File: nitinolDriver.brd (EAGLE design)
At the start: 25 parts

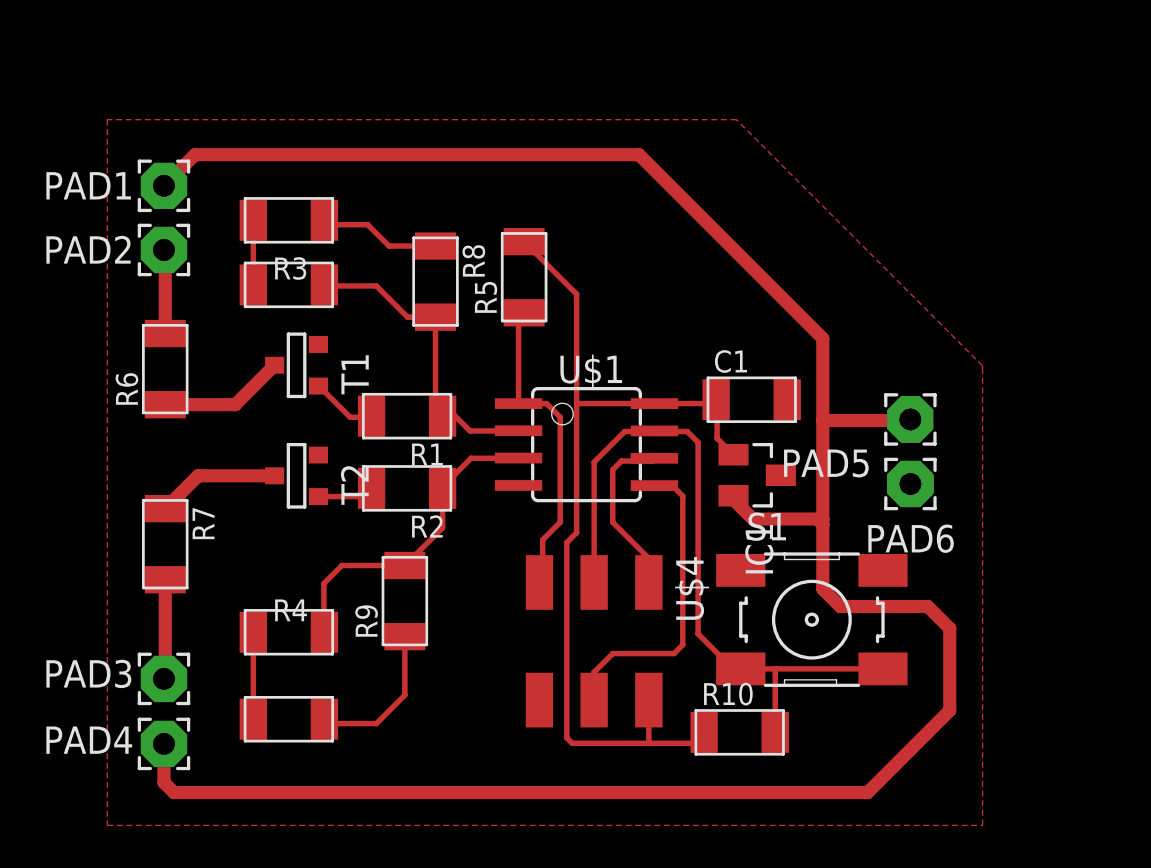
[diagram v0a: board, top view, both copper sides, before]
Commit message: changed to 16A NMOSFETs
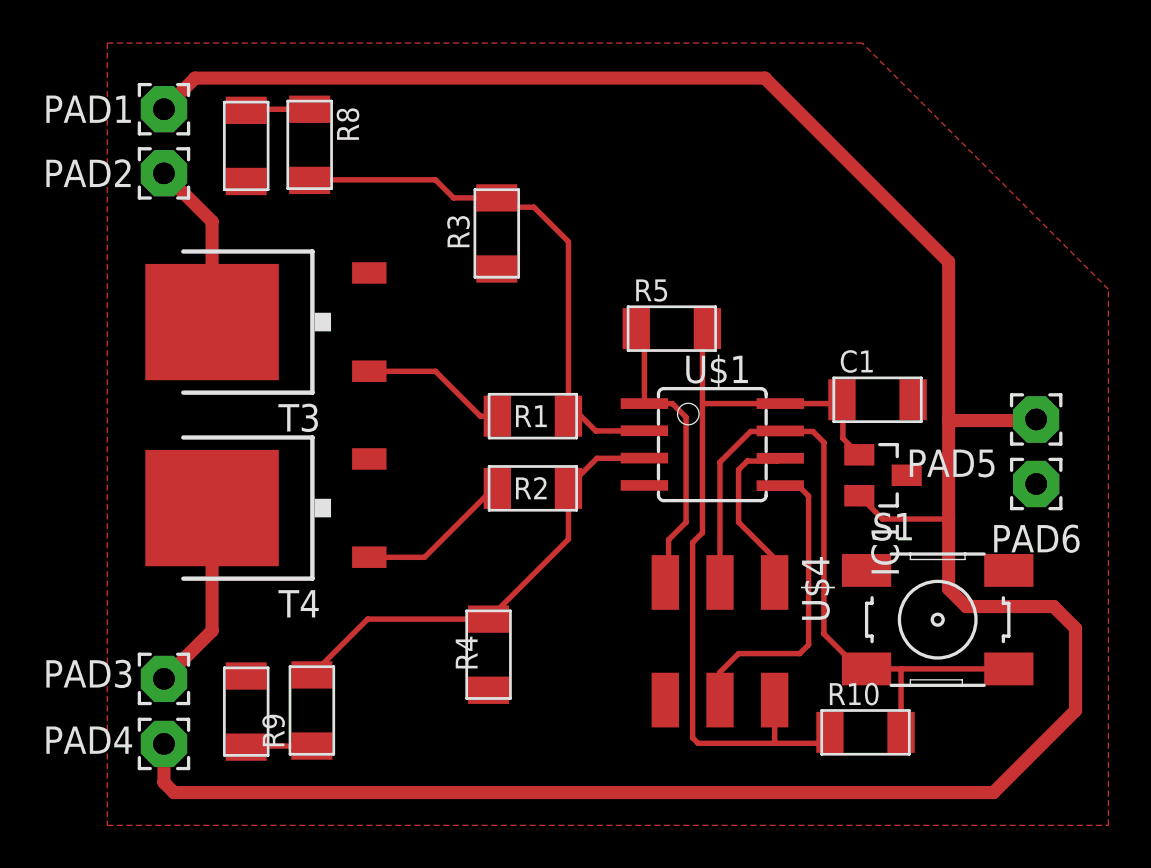
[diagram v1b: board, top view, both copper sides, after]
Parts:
- removed R6, R7: 0, fab:R1206FAB
- removed T1, T2: (no value), fab:SOT-23
- added T3, T4: (no value), fab:TO252
- R1, R2: value 150 -> 100
- moved R3 9.94 mm to (18.6, 33.3), turned to 90 degrees
- moved R4 9.33 mm to (18.2, 13.8), turned to 90 degrees
- moved R8 8.63 mm to (9.91, 37.4)
- moved R5 7.26 mm to (26.7, 28.9), turned to 0 degrees
- moved R9 6.67 mm to (10.0, 11.2)
- moved R1 5.84 mm to (20.3, 24.8)
- moved R10 5.84 mm to (35.7, 10.2)
- moved R2 5.84 mm to (20.3, 21.5)
- moved C1 5.84 mm to (36.3, 25.6)
- moved IC1 5.84 mm to (36.5, 22.1)
- moved PAD5 5.84 mm to (43.6, 24.7)
- moved PAD6 5.84 mm to (43.6, 21.7)
- moved S1 5.84 mm to (39.1, 15.4)
- moved U$1 5.84 mm to (28.6, 23.5)
- moved U$4 5.84 mm to (29.0, 14.6)
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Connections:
- removed net N$5: PAD4.1, R7.2
- removed net N$8: PAD2.1, R6.2
- net GND: now also T3.2, T4.2; no longer T1.2, T2.2
- net N$1: now also R2.2, T4.1; no longer R1.2, T1.3
- net N$11: now also PAD4.1, T4.3; no longer R7.1, T2.1
- net N$14: now also PAD2.1, T3.3; no longer R6.1, T1.1
- net N$2: now also R1.2, T3.1; no longer R2.2, T2.3
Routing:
- net V+: track 105.8 -> 121.0 mm
- net MOSFET1: track 14.3 -> 25.1 mm
- net GND: track 7.29 -> 0.00 mm
- net MOSFET2: track 14.8 -> 21.0 mm
- net VCC: track 42.4 -> 37.4 mm
- net N$5: track 4.63 -> 0.00 mm
- net N$1: track 3.08 -> 7.27 mm
- net N$2: track 2.62 -> 6.81 mm
- net N$4: track 7.08 -> 3.07 mm
- net N$8: track 3.94 -> 0.00 mm
- net N$11: track 5.71 -> 8.86 mm
- net N$3: track 5.65 -> 2.97 mm
- net N$14: track 5.84 -> 7.83 mm
- net RST: track 14.6 -> 13.9 mm
